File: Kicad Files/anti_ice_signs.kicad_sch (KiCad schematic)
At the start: 10 parts, among them SW3 ANTI_ICE_WING_SW, SW4 ANTI_ICE_ENG1_SW, SW5 ANTI_ICE_ENG2_SW

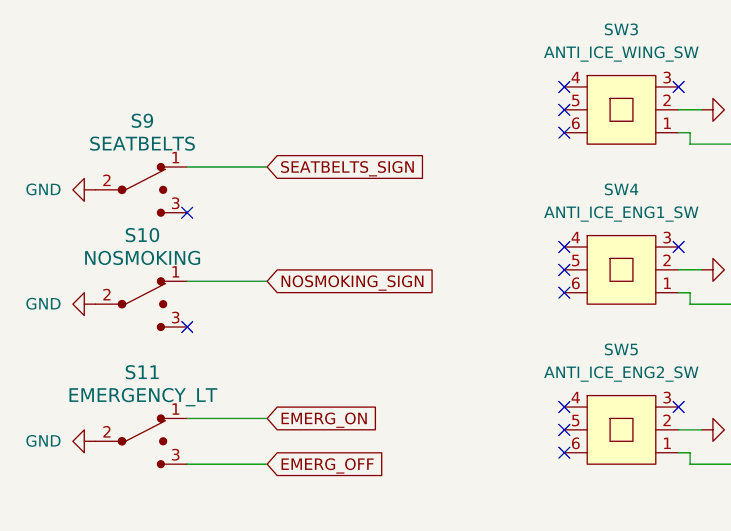
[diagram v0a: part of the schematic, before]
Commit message: Put back the v1 project as it was sent to JLCPCB, with the rotaries fixed
The board in the panel was ordered on 3 March 2025. The Gerbers uploaded to
JLCPCB for that order are byte-identical to production/OverHead_v1.zip,
exported that evening at 22:08. KiCad backed the project up at 22:06 and
at 22:26, with the same copper in both. This restores the 22:26 snapshot:
the board, the schematic sheets and the project files.

Its one flaw is in the file, not in the copper. On 22 February the three
ADIRS rotaries used SimPanel:Rotary_SW_8x1_SF, the footprint made for the
switches actually bought, whose pins sit one position round. By 3 March an
update from the schematic had put the library Rotary_SW_8x1 back under
the same tracks. The copper still reached the right physical pins, but the
file showed nine nets unconnected. The three footprints are taken back from
the 22 February board, with the same position, symbol link and nets. The
schematic now names _SF too, so the next update cannot undo it.

Checked on the result: the DRC finds 0 unconnected items. Following the
copper rather than the net names, each of the 49 buttons in the .mfmc
reaches exactly one switch contact, and each of the 44 annunciator outputs
reaches exactly one LED. The two "shorts" the DRC reports are copper the
schematic never drew: NO SMOKING's contact 3 on D5 and SEAT BELTS'
contact 3 on D18. The .mfmc reads NO SMOKING on D5, so the copper is what
works.

Co-Authored-By: Claude Opus 5.5 <noreply@anthropic.com>
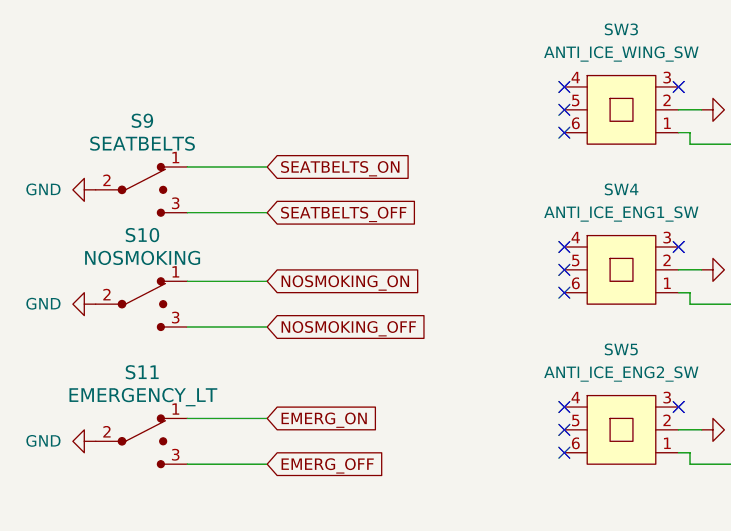
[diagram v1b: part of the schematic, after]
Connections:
- net SEATBELTS_OFF: now reaches S9.3
- net NOSMOKING_OFF: now reaches S10.3
- net NOSMOKING_SIGN renamed NOSMOKING_ON
- net SEATBELTS_SIGN renamed SEATBELTS_ON
- no-connect marks 14 -> 12
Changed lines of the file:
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@@
-	)
-	(no_connect
-		(at 57.15 64.77)
 	)
 	(no_connect
@@
 	)
 	(no_connect
-		(at 57.15 77.47)
-	)
-	(no_connect
 		(at 99.06 53.34)
 	)
@@
 	(wire
 		(pts
+			(xy 66.04 77.47) (xy 57.15 77.47)
+		)
+		(stroke
+			(width 0)
+			(type default)
+		)
+	)
+	(wire
+		(pts
 			(xy 113.03 91.44) (xy 111.76 91.44)
 		)
@@
 	(wire
 		(pts
+			(xy 66.04 64.77) (xy 57.15 64.77)
+		)
+		(stroke
+			(width 0)
+			(type default)
+		)
+	)
+	(wire
+		(pts
 			(xy 66.04 87.63) (xy 57.15 87.63)
 		)
@@
 		)
 	)
-	(global_label "NOSMOKING_SIGN"
+	(global_label "NOSMOKING_ON"
 		(shape input)
 		(at 66.04 72.39 0)
@@
 		)
 		(property "Intersheetrefs" "${INTERSHEET_REFS}"
-			(at 85.5353 72.39 0)
-			(effects
-				(font
-					(size 1.27 1.27)
-				)
-				(justify left)
-				(hide yes)
-			)
-		)
-	)
-	(global_label "SEATBELTS_SIGN"
+			(at 83.7815 72.39 0)
+			(effects
+				(font
+					(size 1.27 1.27)
+				)
+				(justify left)
+				(hide yes)
+			)
+		)
+	)
+	(global_label "SEATBELTS_ON"
 		(shape input)
 		(at 66.04 59.69 0)
@@
 		)
 		(property "Intersheetrefs" "${INTERSHEET_REFS}"
-			(at 84.4465 59.69 0)
+			(at 82.6927 59.69 0)
 			(effects
 				(font
@@
 		)
 	)
+	(global_label "SEATBELTS_OFF"
+		(shape input)
+		(at 66.04 64.77 0)
+		(fields_autoplaced yes)
+		(effects
+			(font
+				(size 1.27 1.27)
+			)
+			(justify left)
+		)
+		(property "Intersheetrefs" "${INTERSHEET_REFS}"
+			(at 83.5394 64.77 0)
+			(effects
+				(font
+					(size 1.27 1.27)
+				)
+				(justify left)
+				(hide yes)
+			)
+		)
+	)
 	(global_label "ANTI_ICE_WING_SW"
 		(shape input)
@@
 			(effects
 				(font
+					(size 1.27 1.27)
+				)
+				(justify left)
+				(hide yes)
+			)
+		)
+	)
+	(global_label "NOSMOKING_OFF"
+		(shape input)
+		(at 66.04 77.47 0)
+		(fields_autoplaced yes)
+		(effects
+			(font
+				(size 1.27 1.27)
+			)
+			(justify left)
+		)
+		(property "Intersheetrefs" "${INTERSHEET_REFS}"
+			(at 84.6282 77.47 0)
+			(effects
+				(font
